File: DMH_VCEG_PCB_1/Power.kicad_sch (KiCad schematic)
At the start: 60 parts, among them J100 IDC_02x08, U1 TL074, U10 TL074, U11 4001, U12 40106, U13 CD4066BE, U14 TL074, U15 TL074, U16 TL074, U17 TL074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

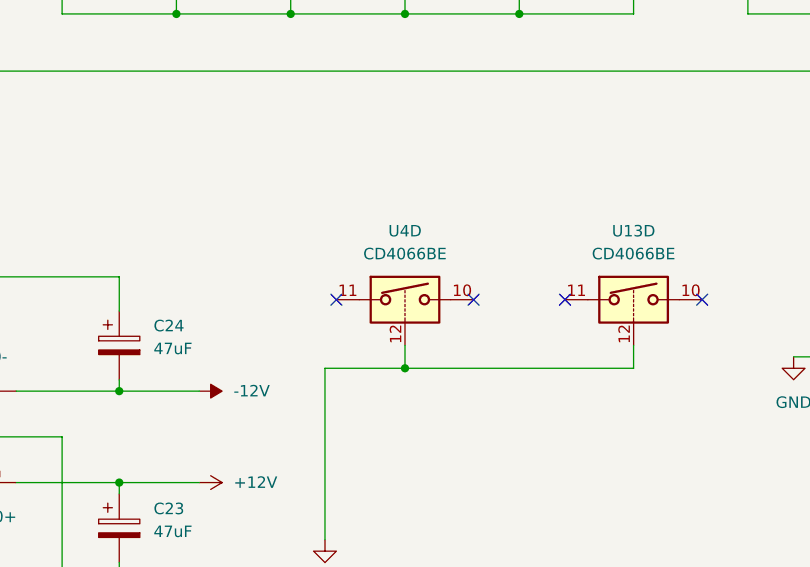
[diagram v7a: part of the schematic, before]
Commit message: Redesign A almost finished
Need to update the Out R to use Release Current Mirror
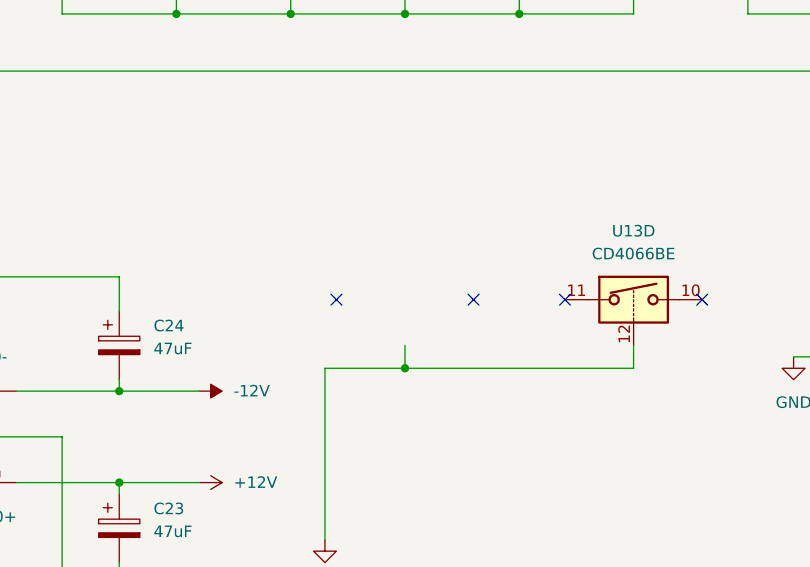
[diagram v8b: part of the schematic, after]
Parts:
- removed unit 4 of U4
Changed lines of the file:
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@@
-	)
-	(symbol
-		(lib_id "Analog_Switch:CD4066BE")
-		(at 88.9 165.1 0)
-		(unit 4)
-		(exclude_from_sim no)
-		(in_bom yes)
-		(on_board yes)
-		(dnp no)
-		(fields_autoplaced yes)
-		(property "Reference" "U4"
-			(at 88.9 157.48 0)
-			(effects
-				(font
-					(size 1.27 1.27)
-				)
-			)
-		)
-		(property "Value" "CD4066BE"
-			(at 88.9 160.02 0)
-			(effects
-				(font
-					(size 1.27 1.27)
-				)
-			)
-		)
-		(property "Footprint" "Package_DIP:DIP-14_W7.62mm"
-			(at 88.9 167.64 0)
-			(effects
-				(font
-					(size 1.27 1.27)
-				)
-				(hide yes)
-			)
-		)
-		(property "Datasheet" "https://www.ti.com/lit/ds/symlink/cd4066b.pdf"
-			(at 88.9 165.1 0)
-			(effects
-				(font
-					(size 1.27 1.27)
-				)
-				(hide yes)
-			)
-		)
-		(property "Description" "Quad 20V analog SPST 1:1 switch, DIP-14"
-			(at 88.9 165.1 0)
-			(effects
-				(font
-					(size 1.27 1.27)
-				)
-				(hide yes)
-			)
-		)
-		(pin "9"
-		)
-		(pin "1"
-		)
-		(pin "7"
-		)
-		(pin "11"
-		)
-		(pin "12"
-		)
-		(pin "6"
-		)
-		(pin "8"
-		)
-		(pin "2"
-		)
-		(pin "10"
-		)
-		(pin "14"
-		)
-		(pin "4"
-		)
-		(pin "13"
-		)
-		(pin "3"
-		)
-		(pin "5"
-		)
-		(instances
-			(project ""
-				(path "/58f4306d-5387-4983-bb08-41a2313fd315/0cdf34b2-39cd-4d9e-981a-97cd34791509"
-					(reference "U4")
-					(unit 4)
-				)
-			)
-		)
 	)
 	(symbol
@@
 			)
 		)
+		(property "Function" ""
+			(at 88.9 50.8 0)
+			(effects
+				(font
+					(size 1.27 1.27)
+				)
+			)
+		)
